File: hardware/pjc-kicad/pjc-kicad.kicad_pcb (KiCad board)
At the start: 2 copper layers, 88 parts, among them CON1 USB-MINI-B, CON10 CONN_2, CON2 CONN_3, CON3 CONN_2, CON4 M023.5MM, CON5 4PIN_FAN_CONN, CON6 CONN_2, CON7 CONN_2, CON8 AVR-ISP-10, CON9 CONN_2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

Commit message: Layout:  almost there...
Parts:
- moved R17 260.4 mm to (119.4, 120.7), turned to 180 degrees
- moved TP2 243.6 mm to (116.8, 134.6)
- moved C10 242.0 mm to (177.8, 77.2), turned to 180 degrees
- moved U9 240.3 mm to (139.7, 141.6), turned to 90 degrees
- moved C14 239.8 mm to (139.7, 134.0), turned to 0 degrees
- moved U2 239.8 mm to (111.8, 130.8)
- moved CON2 239.7 mm to (156.0, 143.3)
- moved Q1 239.4 mm to (194.3, 114.3), turned to 0 degrees
- moved C6 239.0 mm to (104.1, 130.0)
- moved R1 238.0 mm to (153.7, 135.9)
- moved C11 236.6 mm to (177.8, 83.6)
- moved CON3 235.5 mm to (127.0, 144.8)
- moved R4 234.5 mm to (120.7, 130.8), turned to 90 degrees
- moved R3 234.3 mm to (127.0, 130.8)
- moved R2 233.9 mm to (115.6, 143.5)
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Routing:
- net /UART_TX: track 0.00 -> 53.3 mm
- net /UART_RX: track 0.00 -> 48.6 mm
- net /ANA_12V_FB: track 11.5 -> 56.3 mm
- net +5V: track 217.1 -> 248.4 mm
- net +12V: track 42.7 -> 19.1 mm
- net N-0000052: track 0.00 -> 22.4 mm, vias 0 -> 1
- net +5V_USB: track 7.34 -> 28.7 mm
- net N-0000068: track 0.00 -> 18.2 mm
- net /~ADC_CS: track 15.9 -> 32.4 mm
- net /PROJECTOR_ON: track 25.1 -> 39.7 mm
- net /SCK: track 72.9 -> 86.6 mm
- net /MISO: track 65.0 -> 78.3 mm
- net N-0000057: track 14.0 -> 26.3 mm
- net N-000008: track 35.2 -> 25.0 mm
- net N-0000015: track 31.8 -> 22.3 mm
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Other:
- board outline added: 113 x 106.7 mm

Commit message: Layout:  Almost there...
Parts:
- moved CON1 1.27 mm to (201.9, 129.3)
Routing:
- net GND: track 85.9 -> 271.5 mm, vias 1 -> 18
- net +12V: track 19.1 -> 86.1 mm
- net N-0000044: track 22.1 -> 20.8 mm
- net N-0000027: track 22.1 -> 20.8 mm
- net N-0000026: track 23.2 -> 22.0 mm
- added copper zone on F.Cu, net +12V
- added copper zone on B.Cu, net GND
- added copper zone on F.Cu, net GND
- added copper zone on F.Cu, net N-0000064
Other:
- board size 113 x 106.7 mm -> 110.5 x 104.1 mm

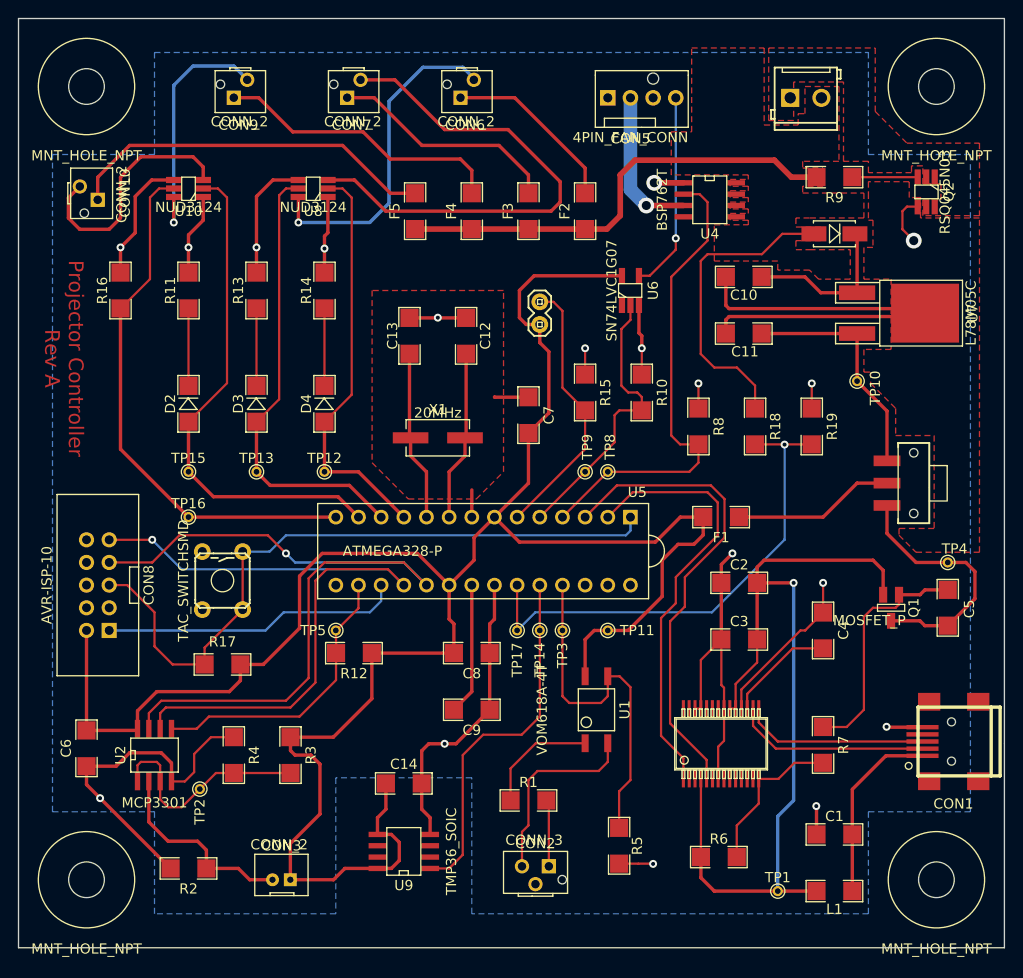
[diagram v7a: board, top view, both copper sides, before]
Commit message: Board layout done!
Need to change NPTH mechanical holes to PTH holes since KiCad generates a second drill file for NPTH holes, which won't work.
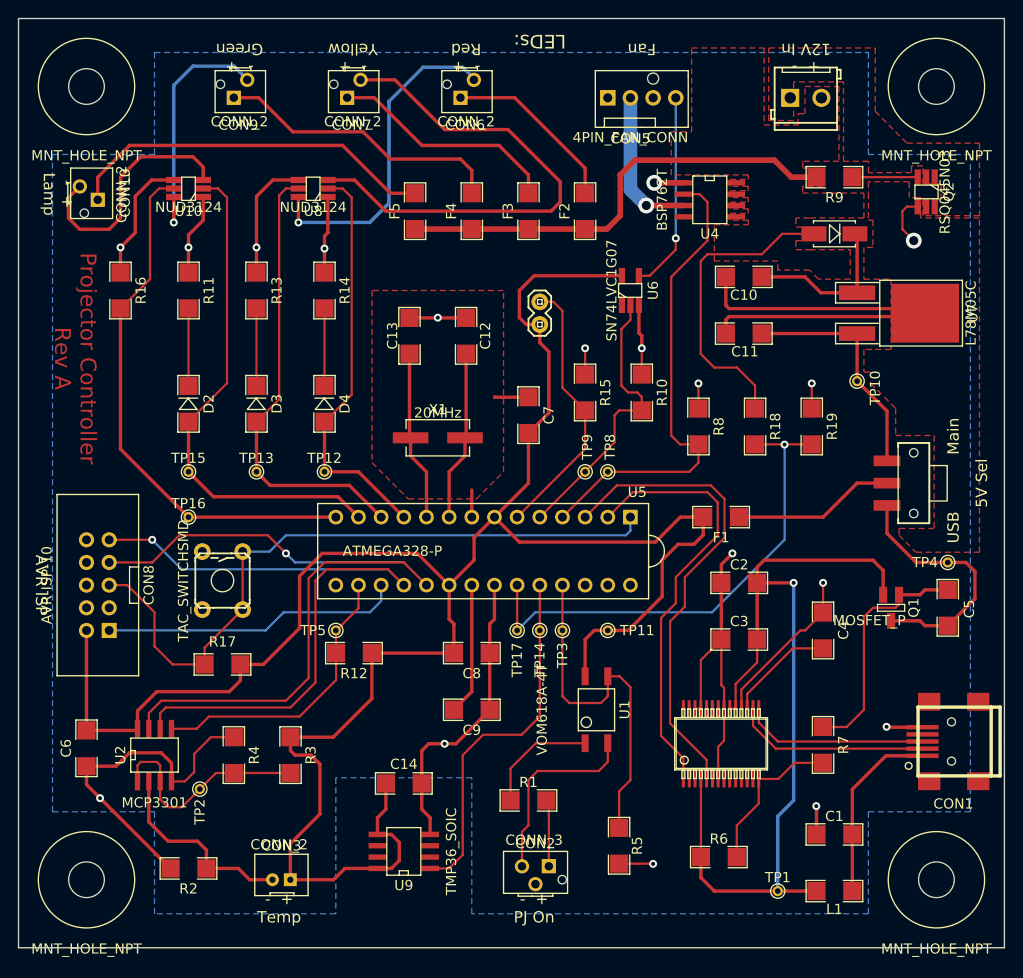
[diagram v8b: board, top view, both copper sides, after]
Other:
- net class Default: clearance 0.254 -> 0.2032
- rule trace_clearance: 0.254 -> 0.2032
- rule trace_min: 0.254 -> 0.2032
- board text added: "+ - 12V In"
- board text added: "- + Green"
- board text added: "- + Lamp"
- board text added: "- + PJ On"
- board text added: "- + Red"
- board text added: "- + Temp"
- board text added: "- + Yellow"
- board text added: "5V Sel"
- board text added: "AVR ISP"
- board text added: "Fan"
- board text added: "LEDs:"
- board text added: "Main"
- board text added: "USB"
